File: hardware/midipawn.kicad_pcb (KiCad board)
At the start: 4 copper layers, 134 x 86.4 mm, 82 parts, among them J1 MIDI I/O, J10 LOOP 8, J11 LOOP 9, J12 LOOP 10, J13 Barrel_Jack_Switch, J2 I/O, J3 LOOP 1, J4 LOOP 2, J5 LOOP 3, J6 LOOP 4, J7 LOOP 5, J8 LOOP 6, J9 LOOP 7, K1 G6S-2, K10 G6S-2, K2 G6S-2, K3 G6S-2, K4 G6S-2, K5 G6S-2, K6 G6S-2, K7 G6S-2, K8 G6S-2, K9 G6S-2, Q1 2N3904, Q10 2N3904, Q2 2N3904, Q3 2N3904, Q4 2N3904, Q5 2N3904, Q6 2N3904, Q7 2N3904, Q8 2N3904, Q9 2N3904, U1 L7805, U2 6N137

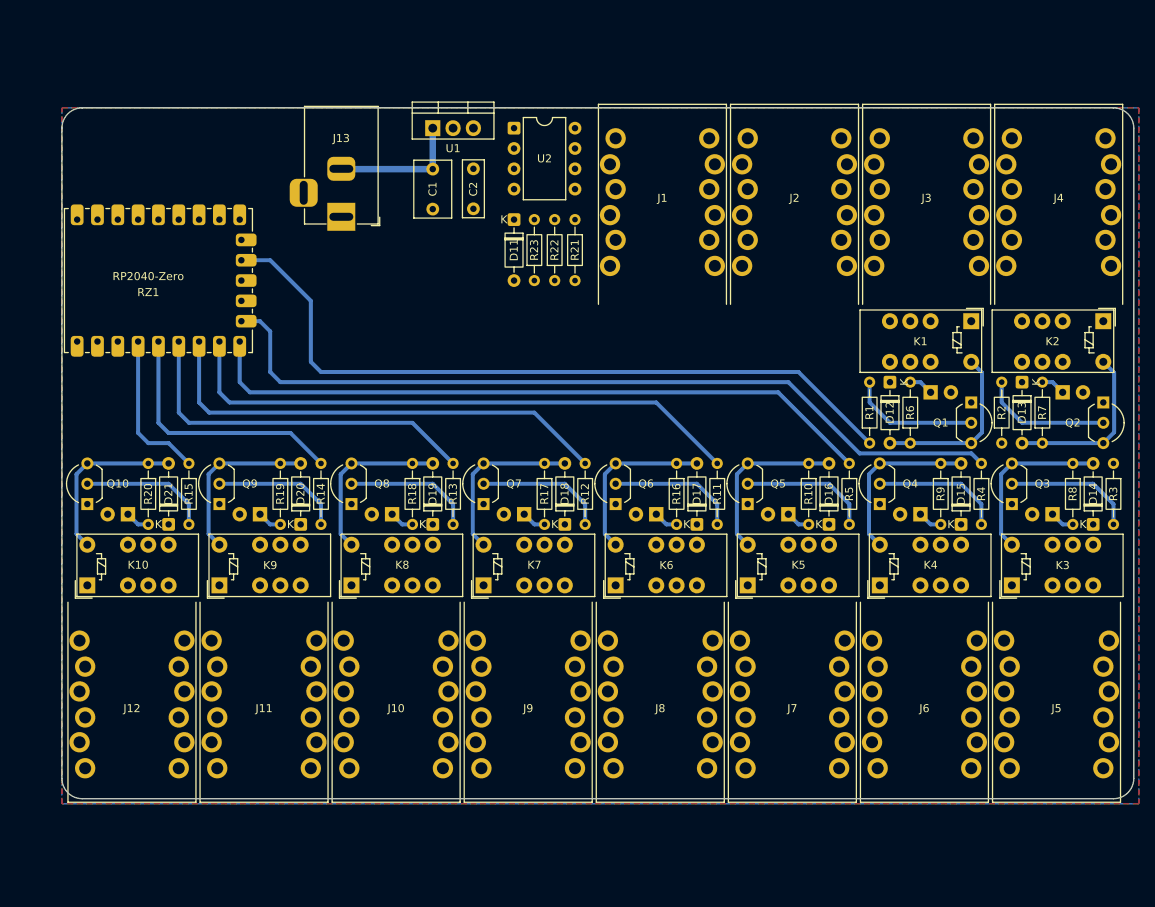
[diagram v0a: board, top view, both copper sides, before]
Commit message: Add STEP 3D model for audio jacks connector
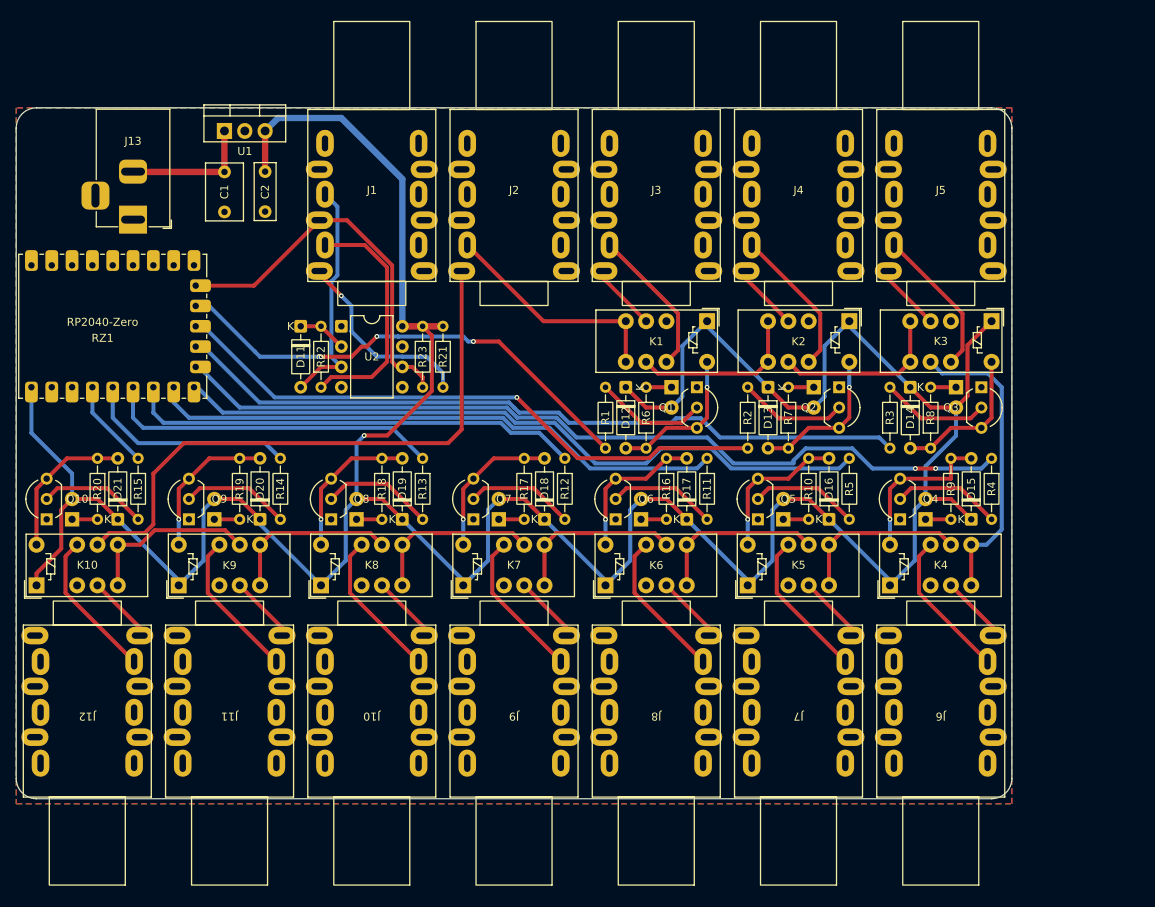
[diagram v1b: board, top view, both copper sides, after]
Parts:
- moved J5 65.4 mm to (195.6, 69.2), turned to 0 degrees
- moved J1 36.3 mm to (124.5, 69.2)
- moved J2 35.1 mm to (142.2, 69.2)
- moved Q1 34.3 mm to (165.1, 93.3)
- moved J3 33.8 mm to (160.0, 69.2)
- moved K3 33.1 mm to (201.9, 85.1), turned to -90 degrees
- moved Q2 33.1 mm to (182.9, 93.3)
- moved R1 33.0 mm to (153.7, 101.0)
- moved R6 33.0 mm to (158.8, 101.0)
- moved D12 33.0 mm to (156.2, 93.3)
- moved K1 33.0 mm to (166.4, 85.1)
- moved U2 32.9 mm to (120.7, 85.7)
- moved J4 32.5 mm to (177.8, 69.2)
- moved D1 32.4 mm to (161.9, 93.3), turned to -90 degrees
- moved R22 32.1 mm to (118.1, 93.3)
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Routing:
- net +5V: track 0.00 -> 391.6 mm, vias 0 -> 1
- net MCU_LOOP1: track 92.5 -> 60.7 mm, vias 0 -> 3
- net MCU_LOOP2: track 107.2 -> 76.4 mm, vias 0 -> 1
- net MCU_LOOP3: track 121.1 -> 92.5 mm
- net Net-(J1-T): track 9.72 -> 30.3 mm
- net Net-(J1-2T): track 5.14 -> 24.6 mm, vias 0 -> 1
- net OUT: track 94.2 -> 75.0 mm
- net OUT_LOOP3: track 20.4 -> 37.7 mm
- net OUT_LOOP2: track 37.9 -> 21.5 mm
- net Net-(D11-A): track 41.2 -> 29.2 mm
- net Net-(D11-K): track 16.0 -> 6.13 mm
- net MCU_MIDI: track 56.8 -> 48.2 mm
- net MCU_LOOP10: track 19.4 -> 11.3 mm
- net MCU_LOOP9: track 32.6 -> 26.9 mm
- net MCU_LOOP4: track 102.8 -> 107.0 mm, vias 0 -> 2
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- added copper zone on B.Cu, net GND
- removed copper zone on B.Cu, net +5V
- removed copper zone on In1.Cu, net GND
- removed copper zone on In2.Cu, net GND
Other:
- board size 134 x 86.4 mm -> 124.5 x 86.4 mm
- copper layers 4 -> 2

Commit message: Adjust audio jack positions to align with board edge
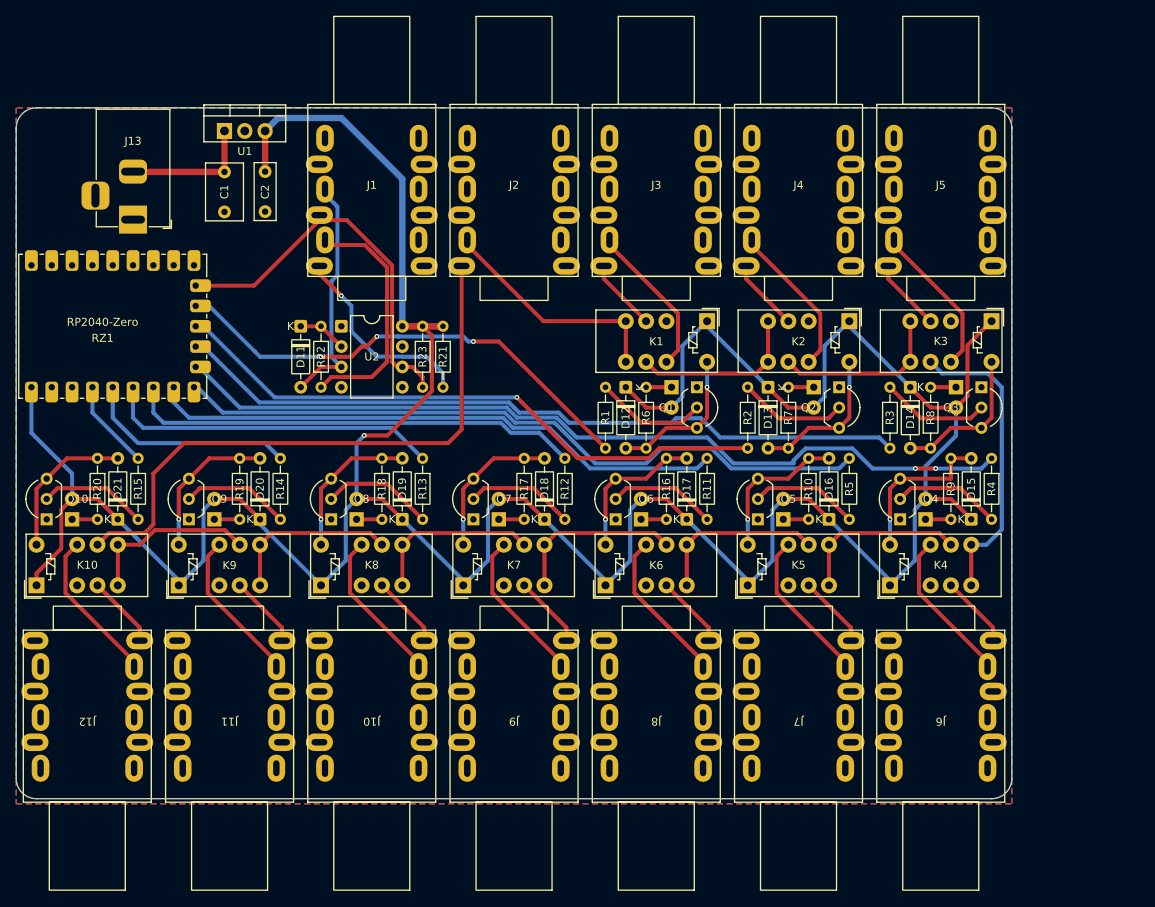
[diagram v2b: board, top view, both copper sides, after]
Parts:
- moved J1 0.64 mm to (124.5, 68.6)
- moved J2 0.64 mm to (142.2, 68.6)
- moved J3 0.64 mm to (160.0, 68.6)
- moved J4 0.64 mm to (177.8, 68.6)
- moved J5 0.64 mm to (195.6, 68.6)
- moved J10 0.63 mm to (124.5, 134.6)
- moved J11 0.63 mm to (106.7, 134.6)
- moved J12 0.63 mm to (88.9, 134.6)
- moved J6 0.63 mm to (195.6, 134.6)
- moved J7 0.63 mm to (177.8, 134.6)
- moved J8 0.63 mm to (160.0, 134.6)
- moved J9 0.63 mm to (142.2, 134.6)
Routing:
- net MCU_MIDI: track 48.2 -> 49.1 mm
- net Net-(J9-T): track 18.8 -> 19.4 mm
- net Net-(J8-T): track 18.8 -> 19.4 mm
- net Net-(J7-T): track 18.8 -> 19.4 mm
- net Net-(J6-T): track 18.8 -> 19.4 mm
- net Net-(J12-T): track 18.8 -> 19.4 mm
- net Net-(J11-T): track 18.8 -> 19.4 mm
- net Net-(J10-T): track 18.8 -> 19.4 mm
- net Net-(D11-A): track 29.2 -> 29.8 mm
- net Net-(J3-T): track 18.8 -> 19.4 mm
- net OUT: track 75.0 -> 75.7 mm
- net Net-(J9-2T): track 8.46 -> 9.10 mm
- net Net-(J8-2T): track 8.46 -> 9.10 mm
- net Net-(J7-2T): track 8.46 -> 9.10 mm
- net Net-(J6-2T): track 8.46 -> 9.10 mm
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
